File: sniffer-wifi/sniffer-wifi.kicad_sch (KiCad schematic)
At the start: 48 parts, among them J1 USB_B_Micro, J2 Conn_01x05_Socket, J3 Screw_Terminal_01x02, J4 Screw_Terminal_01x02, J5 Conn_02x04_Odd_Even, Q1 BC547, Q2 BC547, Q3 BC547, U1 ATmega328PB-A, U2 LF33_TO220, Y1 18.4320 MHz

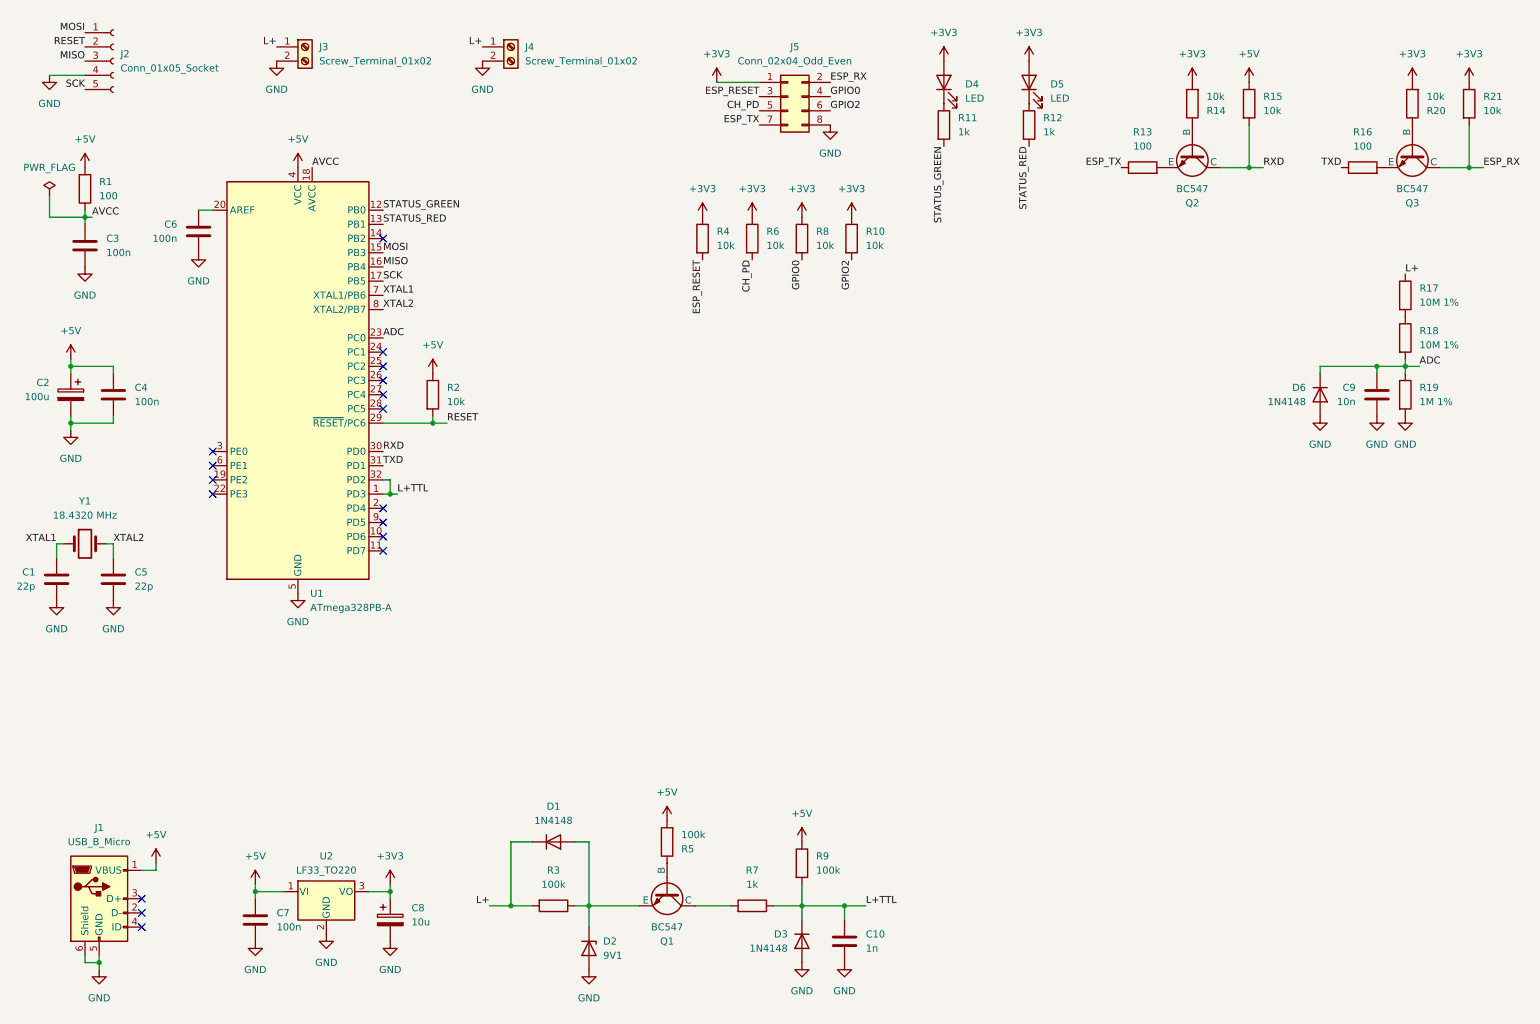
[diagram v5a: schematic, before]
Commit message: add ferrite beads, power down control pin, current probe jumper, replace mcu
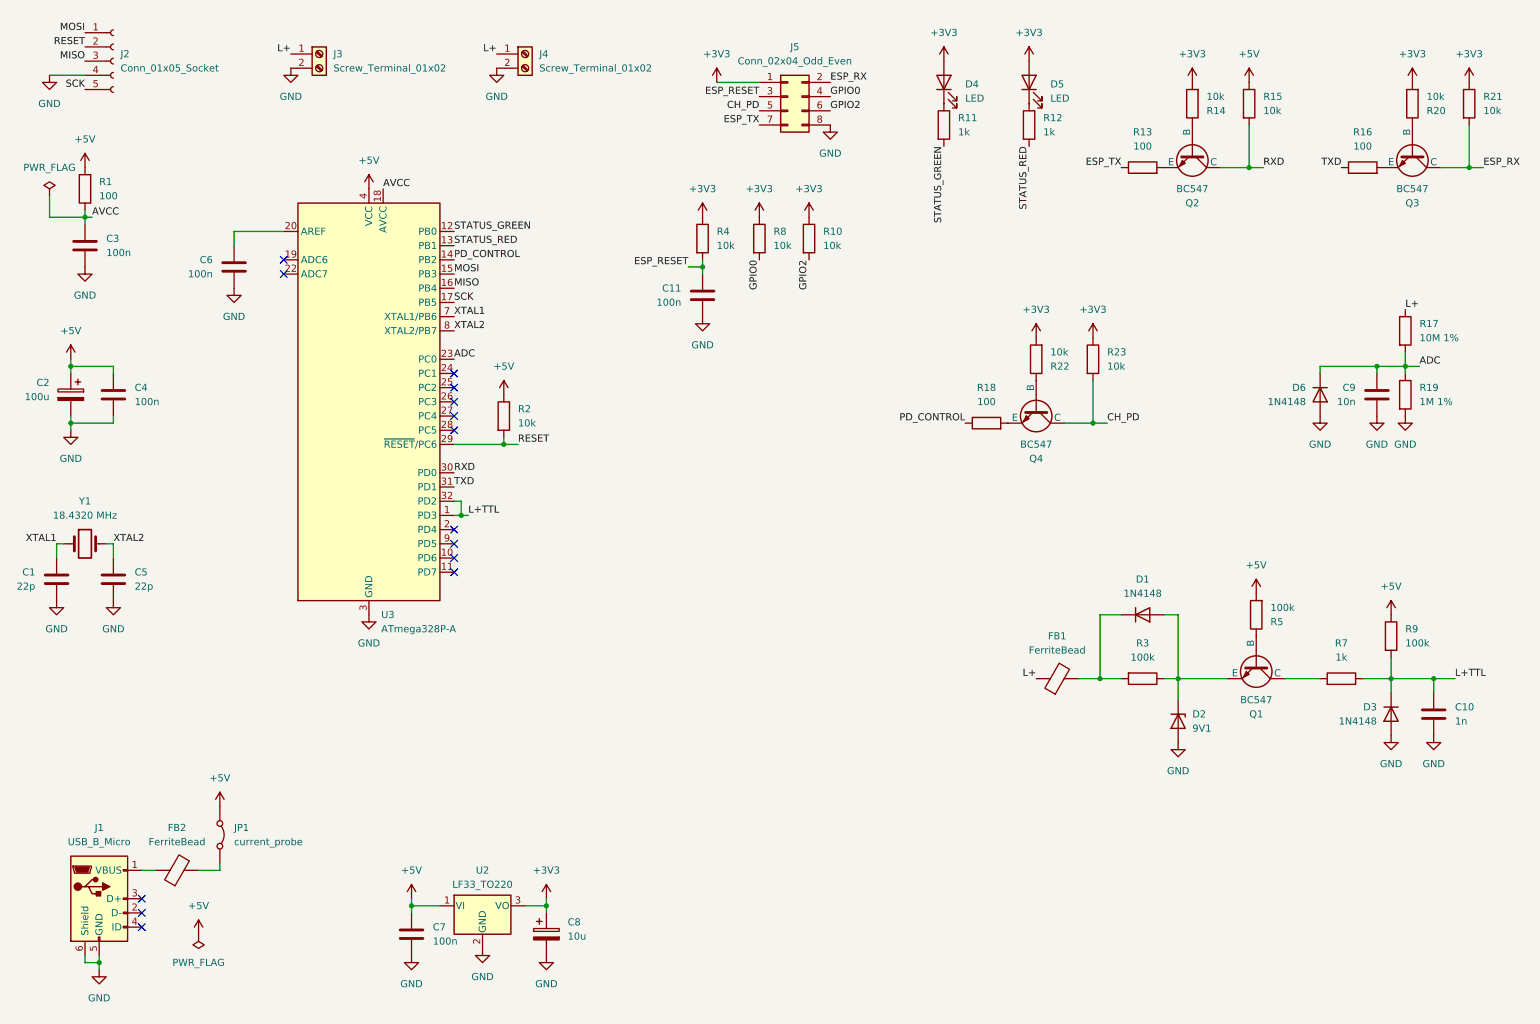
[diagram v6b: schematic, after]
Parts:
- removed R6: 10k, symbol Device:R
- removed U1: ATmega328PB-A, Package_QFP:TQFP-32_7x7mm_P0.8mm, symbol MCU_Microchip_ATmega:ATmega328PB-A
- added C11: 100n, symbol Device:C
- added FB1, FB2: FerriteBead, symbol Device:FerriteBead
- added JP1: current_probe, symbol Jumper:Jumper_2_Bridged
- added Q4: BC547, Package_TO_SOT_THT:TO-92, symbol Simulation_SPICE:NPN
- added R22, R23: 10k, symbol Device:R
- added U3: ATmega328P-A, Package_QFP:TQFP-32_7x7mm_P0.8mm, symbol MCU_Microchip_ATmega:ATmega328P-A
- R18: value 10M 1% -> 100
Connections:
- net +3V3: now also R22.2, R23.1
- net +5V: now also JP1.1 (A), U3.4 (VCC), U3.6 (VCC); no longer J1.1 (VBUS)
- net ADC: now also R17.2, U3.23 (PC0); no longer R18.2
- net AVCC: now also U3.18 (AVCC)
- net CH_PD: now also Q4.1 (C), R23.2
- net ESP_RESET: now also C11.1
- net GND: now also C11.2, U3.21 (GND), U3.3 (GND), U3.5 (GND)
- net L+: now also FB1.1; no longer D1.1 (K), R3.2
- net L+TTL: now also U3.1 (PD3), U3.32 (PD2)
- net MISO: now also U3.16 (PB4)
- net MOSI: now also U3.15 (PB3)
- net RESET: now also U3.29 (~{RESET}/PC6)
- net RXD: now also U3.30 (PD0)
- net SCK: now also U3.17 (PB5)
- net STATUS_GREEN: now also U3.12 (PB0)
- net STATUS_RED: now also U3.13 (PB1)
- net TXD: now also U3.31 (PD1)
- net XTAL1: now also U3.7 (XTAL1/PB6)
- net XTAL2: now also U3.8 (XTAL2/PB7)
- net at C6.1: now also U3.20 (AREF)
- net PD_CONTROL: now reaches R18.1
- net PD_CONTROL: now also U3.14 (PB2); no longer R17.2
- new net: D1.1 (K), FB1.2, R3.2
- new net: Q4.2 (B), R22.1
- new net: Q4.3 (E), R18.2
- new net: FB2.1, J1.1 (VBUS)
- new net: FB2.2, JP1.2 (B)
- no-connect marks 17 -> 14
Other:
- moved on the sheet: C10, C6, C7, C8, D1, D2, D3, J3, J4, Q1, R10, R17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

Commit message: Add files via upload
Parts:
- removed C10: 1n, symbol Device:C
- removed FB1: FerriteBead, symbol Device:FerriteBead
- added C12: 100p, symbol Device:C
- added C13: 1n, symbol Device:C
- added FB3, FB4: FerriteBead, symbol Device:FerriteBead
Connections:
- net GND: now also C12.2, C13.2, FB4.1; no longer J3.2 (Pin_2), J4.2 (Pin_2)
- net L+: now also D1.1 (K), R3.2, FB3.1; no longer J3.1 (Pin_1), J4.1 (Pin_1)
- net L+TTL: now also C13.1
- net at D1.2 (A), D2.1 (K), Q1.3 (E)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: now also C12.1
- new net: FB3.2, J3.1 (Pin_1), J4.1 (Pin_1)
- new net: FB4.2, J3.2 (Pin_2), J4.2 (Pin_2)
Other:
- moved on the sheet: D1, D2, J3, J4, R3

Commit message: Add files via upload
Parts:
- removed C8: 10u, symbol Device:C_Polarized
- removed D2: 9V1, symbol Device:D_Zener
- removed D3, D6: 1N4148, symbol Device:D
- removed Q1, Q2, Q3, Q4: BC547, Package_TO_SOT_THT:TO-92, symbol Simulation_SPICE:NPN
- removed R1: 100, symbol Device:R
- removed U2: LF33_TO220, Package_TO_SOT_THT:TO-220-3_Vertical, symbol Regulator_Linear:LF33_TO220
- removed Y1: 18.4320 MHz, symbol Device:Crystal
- added C10, C14, C15: 100n, symbol Device:C
- added C8: 10u, symbol Device:C
- added D2, D3: BZV55B6V2, Diode_SMD:D_MiniMELF, symbol Diode:BZV55B6V2
- added D6: BZV55B9V1, Diode_SMD:D_MiniMELF, symbol Diode:BZV55B9V1
- added FB1: FerriteBead, symbol Device:FerriteBead
- added JP2: F7, symbol Jumper:Jumper_2_Open
- added JP3: F6, symbol Jumper:Jumper_2_Open
- added JP4: F5, symbol Jumper:Jumper_2_Open
- added JP5: F4, symbol Jumper:Jumper_2_Open
- added JP6: F3, symbol Jumper:Jumper_2_Open
- added JP7: F2, symbol Jumper:Jumper_2_Open
- added JP8: F1, symbol Jumper:Jumper_2_Open
- added JP9: F0, symbol Jumper:Jumper_2_Open
- added Q1, Q2, Q5: MMBT3904, Package_TO_SOT_SMD:SOT-23, symbol Transistor_BJT:MMBT3904
- added Q6: MMBT5551L, Package_TO_SOT_SMD:SOT-23, symbol Transistor_BJT:MMBT5551L
- added U1: AMS1117-3.3, Package_TO_SOT_SMD:SOT-223-3_TabPin2, symbol Regulator_Linear:AMS1117-3.3
- added Y1: 18.4320M, Crystal:Crystal_SMD_3225-4Pin_3.2x2.5mm, symbol Device:Crystal_GND24
- C1, C5: value 22p -> 12p
- C4: value 100n -> 10u
- U3: value ATmega328P-A -> ATmega328PB
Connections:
- net +3V3: now also C15.1, C8.1, U1.2 (VO)
- net +5V: now also C10.1, C14.1, FB1.2, U1.3 (VI)
- net ADC: now also D2.1 (K)
- net AVCC: now also FB1.1
- net CH_PD: now also Q5.3 (C)
- net ESP_RX: now also Q2.3 (C)
- net GND: now also C10.2, C14.2, C15.2, C8.2, D2.2 (A), D3.2 (A), D6.2 (A), JP2.2 (B), JP3.2 (B), JP4.2 (B), JP5.2 (B), JP6.2 (B), JP7.2 (B), JP8.2 (B), JP9.2 (B), U1.1 (GND), Y1.2, Y1.4
- net L+TTL: now also D3.1 (K)
- net RXD: now also Q1.3 (C)
- net XTAL1: now also Y1.1
- net XTAL2: now also Y1.3
- net at C12.1, D1.2 (A), R3.1: now also D6.1 (K), Q6.2 (E)
- net at R22.1: now also Q5.1 (B)
- net at R18.2: now also Q5.2 (E)
- net at R20.1: now also Q2.1 (B)
- net at R16.2: now also Q2.2 (E)
- net at R5.1: now also Q6.1 (B)
- net at R7.2: now also Q6.3 (C)
- net at R14.1: now also Q1.1 (B)
- net at R13.2: now also Q1.2 (E)
- net F6: now reaches U3.10 (PD6)
- net F6: now also JP3.1 (A)
- net F7: now reaches U3.11 (PD7)
- net F7: now also JP2.1 (A)
- net F4: now reaches U3.2 (PD4)
- net F4: now also JP5.1 (A)
- net F0: now reaches U3.25 (PC2)
- net F0: now also JP9.1 (A)
- net F1: now reaches U3.26 (PC3)
- net F1: now also JP8.1 (A)
- net F2: now reaches U3.27 (PC4)
- net F2: now also JP7.1 (A)
- net F3: now reaches U3.28 (PC5)
- net F3: now also JP6.1 (A)
- net F5: now reaches U3.9 (PD5)
- net F5: now also JP4.1 (A)
- no-connect marks 14 -> 6
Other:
- moved on the sheet: C1, C2, C3, C4, C5, C7
